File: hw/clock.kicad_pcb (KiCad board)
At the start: 2 copper layers, 1 part, among them U1 ATMEGA328PB-AU

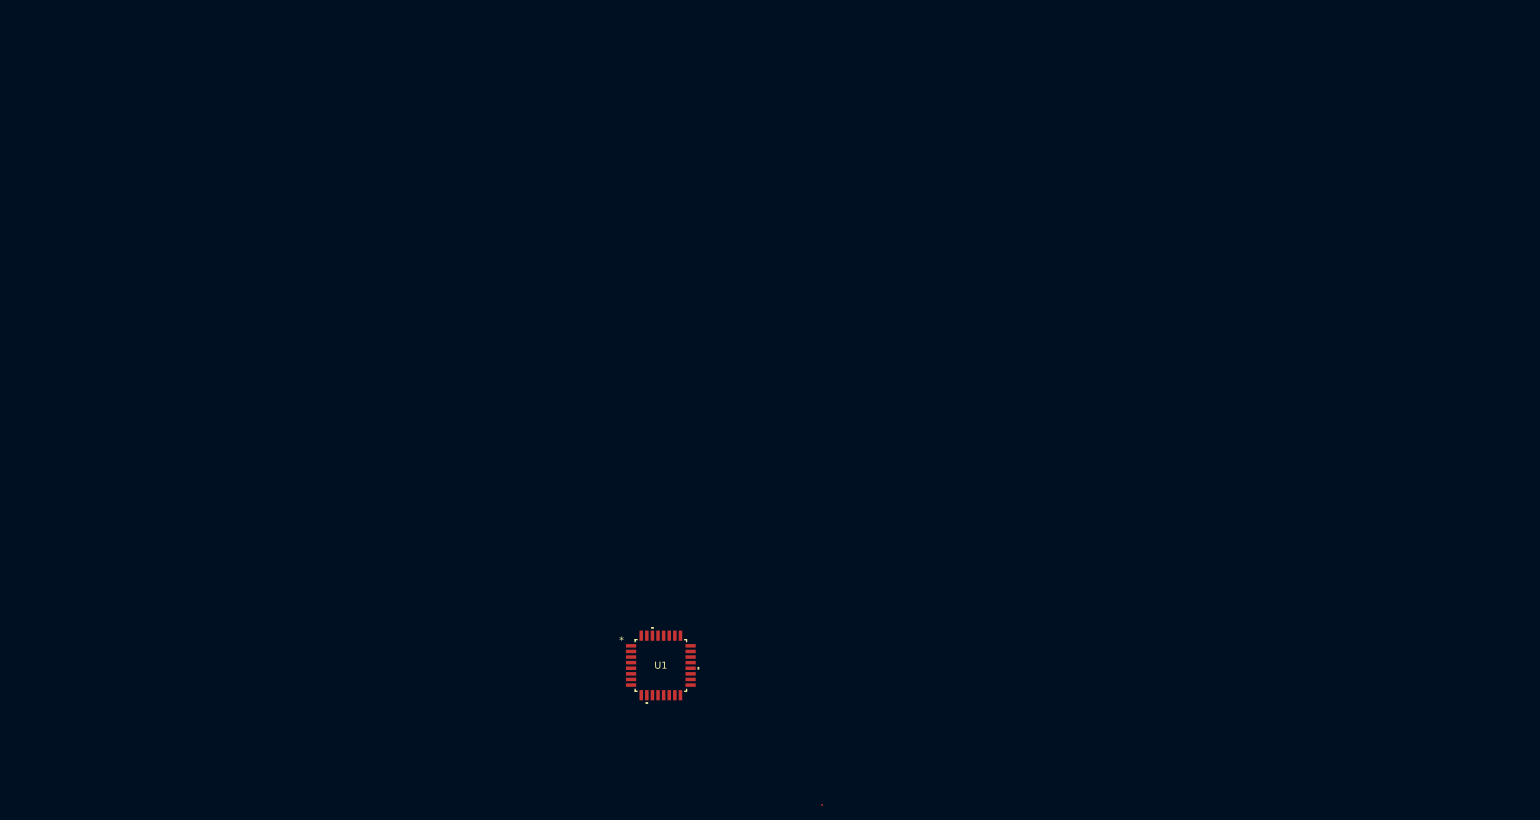
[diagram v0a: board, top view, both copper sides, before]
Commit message: Assign footprints
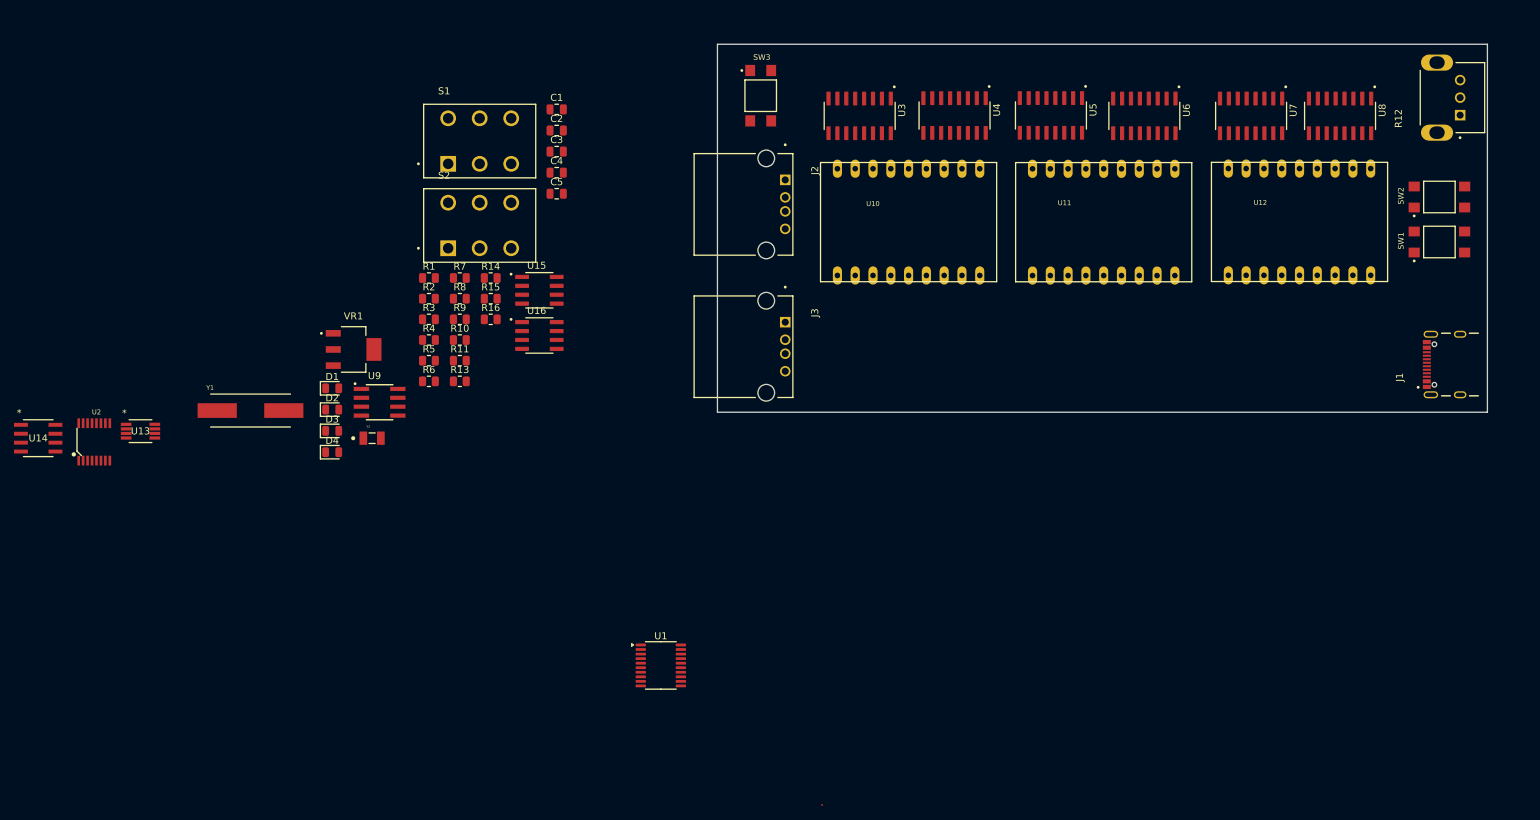
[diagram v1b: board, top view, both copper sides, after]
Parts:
- added C1: 18pf, Capacitor_SMD:C_0805_2012Metric, F.Cu at (117.4, 57.6)
- added C2: 18pf, Capacitor_SMD:C_0805_2012Metric, F.Cu at (117.4, 60.6)
- added C3: 12.5pf, Capacitor_SMD:C_0805_2012Metric, F.Cu at (117.4, 63.6)
- added C4: 12.5pf, Capacitor_SMD:C_0805_2012Metric, F.Cu at (117.4, 66.6)
- added C5: 33uf, Capacitor_SMD:C_0805_2012Metric, F.Cu at (117.4, 69.6)
- added D1: LED, LED_SMD:LED_0805_2012Metric, F.Cu at (85.4, 97.4)
- added D2: LED, LED_SMD:LED_0805_2012Metric, F.Cu at (85.4, 100.4)
- added D3: LED, LED_SMD:LED_0805_2012Metric, F.Cu at (85.4, 103.5)
- added D4: LED, LED_SMD:LED_0805_2012Metric, F.Cu at (85.4, 106.5)
- added J1: USB4105-GF-A, Clock:GCT_USB4105-GF-A, F.Cu at (246.4, 94.0)
- added J2: USB-A1HSW6, Clock:OST_USB-A1HSW6, F.Cu at (147.3, 71.1)
- added J3: USB-A1HSW6, Clock:OST_USB-A1HSW6, F.Cu at (147.3, 91.4)
- added R1: 10k, Resistor_SMD:R_0805_2012Metric, F.Cu at (99.2, 81.6)
- added R10: 10k, Resistor_SMD:R_0805_2012Metric, F.Cu at (103.6, 90.5)
- added R11: 10, Resistor_SMD:R_0805_2012Metric, F.Cu at (103.6, 93.4)
- added R12: PT01-B120D-B102, Clock:TRIM_PT01-B120D-B102, F.Cu at (243.1, 55.9)
- added R13: 10k, Resistor_SMD:R_0805_2012Metric, F.Cu at (103.6, 96.4)
- added R14: 10k, Resistor_SMD:R_0805_2012Metric, F.Cu at (108.0, 81.6)
- added R15: 2m, Resistor_SMD:R_0805_2012Metric, F.Cu at (108.0, 84.6)
- added R16: 2m, Resistor_SMD:R_0805_2012Metric, F.Cu at (108.0, 87.5)
- added R2: 5.1k, Resistor_SMD:R_0805_2012Metric, F.Cu at (99.2, 84.6)
- added R3: 5.1k, Resistor_SMD:R_0805_2012Metric, F.Cu at (99.2, 87.5)
- added R4: 10k, Resistor_SMD:R_0805_2012Metric, F.Cu at (99.2, 90.5)
- added R5: 10k, Resistor_SMD:R_0805_2012Metric, F.Cu at (99.2, 93.4)
- added R6: 10k, Resistor_SMD:R_0805_2012Metric, F.Cu at (99.2, 96.4)
- added R7: 10k, Resistor_SMD:R_0805_2012Metric, F.Cu at (103.6, 81.6)
- added R8: 10k, Resistor_SMD:R_0805_2012Metric, F.Cu at (103.6, 84.6)
- added R9: 10k, Resistor_SMD:R_0805_2012Metric, F.Cu at (103.6, 87.5)
- added S1: SLW-1678105-6A-N-D, Clock:SW_SLW-1678105-6A-N-D, F.Cu at (106.4, 62.1)
- added S2: SLW-1678105-6A-N-D, Clock:SW_SLW-1678105-6A-N-D, F.Cu at (106.4, 74.1)
- added SW1: TL3305AF260QG, Clock:SW_TL3305AF260QG, F.Cu at (243.4, 76.5)
- added SW2: TL3305AF260QG, Clock:SW_TL3305AF260QG, F.Cu at (243.4, 70.1)
- added SW3: TL3305AF260QG, Clock:SW_TL3305AF260QG, F.Cu at (146.5, 55.6)
- added U10: HDSP-5321 Common Anode, Clock:HDSP-R, F.Cu at (167.6, 73.6)
- added U11: HDSP-5321 Common Anode, Clock:HDSP-R, F.Cu at (195.5, 73.7)
- added U12: HDSP-5321 Common Anode, Clock:HDSP-R, F.Cu at (223.4, 73.6)
- added U13: MCP9808T-E/MS, Clock:MCP9808T, F.Cu at (58.0, 103.5)
- added U14: AP2192ASG-13, Clock:AP2192ASG_13, F.Cu at (43.4, 104.5)
- added U15: INA219AIDR, Clock:INA219AIDR, F.Cu at (114.9, 83.4)
- added U16: INA219AIDR, Clock:INA219AIDR, F.Cu at (114.9, 89.8)
- added U2: INTERFACE-FT230XS-R_SSOP16_, Clock:SSOP16-0.635-5X4MM, F.Cu at (51.4, 105.0)
- added U3: SN74HC595DR, Clock:SOIC127P600X175-16N, F.Cu at (160.7, 58.5)
- added U4: SN74HC595DR, Clock:SOIC127P600X175-16N, F.Cu at (174.2, 58.4)
- added U5: SN74HC595DR, Clock:SOIC127P600X175-16N, F.Cu at (188.0, 58.4)
- added U6: SN74HC595DR, Clock:SOIC127P600X175-16N, F.Cu at (201.3, 58.5)
- added U7: SN74HC595DR, Clock:SOIC127P600X175-16N, F.Cu at (216.5, 58.5)
- added U8: SN74HC595DR, Clock:SOIC127P600X175-16N, F.Cu at (229.2, 58.5)
- added U9: MCP7940MT-I_SN, Clock:SOIC127P600X175-8N, F.Cu at (92.1, 99.4)
- added VR1: LM3940IMP-3.3_NOPB, Clock:VREG_LM3940IMP-3.3_NOPB, F.Cu at (88.4, 91.8)
- added Y1: 30MHz, Clock:XTAL_ABLS2-30.000MHZ-D4YF-T, F.Cu at (73.7, 100.5)
- added Y2: 32.768KHz, Clock:XTAL_ECS-.327-12.5-34RR-TR, F.Cu at (91.1, 104.5)
- U1: value ATMEGA328PB-AU -> LPC812M101JDH20; footprint Clock:32A_MCH -> Package_SO:TSSOP-20_4.4x6.5mm_P0.65mm
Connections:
- U1 pad 1: unconnected-(U1-(OC2B/INT1/PTCXY)PD3-Pad1) -> SHIFT_SER_5
- U1 pad 10: unconnected-(U1-(OC0A/PTCXY/AIN0)PD6-Pad10) -> SHIFT_SER_4
- U1 pad 11: unconnected-(U1-(PTCXY/AIN1)PD7-Pad11) -> SHIFT_SER_3
- U1 pad 12: unconnected-(U1-(ICP1/CLKO/PTCXY)PB0-Pad12) -> MODE
- U1 pad 13: unconnected-(U1-(OC1A/PTCXY)PB1-Pad13) -> Net-(U1-PIO0_9)
- U1 pad 14: unconnected-(U1-(*SS0/OC1B/PTCXY)PB2-Pad14) -> Net-(U1-PIO0_8)
- U1 pad 15: unconnected-(U1-(MOSI0/TXD1/OC2A/PTCXY)PB3-Pad15) -> +3V3
- U1 pad 16: unconnected-(U1-(MISO0/RXD1/PTCXY)PB4-Pad16) -> +5V
- U1 pad 17: unconnected-(U1-(PTCXY/XCK1/SCK0)PB5-Pad17) -> SHIFT_SER_6
- U1 pad 18: unconnected-(U1-AVCC-Pad18) -> SHIFT_CLK
- U1 pad 19: unconnected-(U1-(ADC6/PTCY/ICP3/*SS1)PE2-Pad19) -> SERIAL1
- U1 pad 2: unconnected-(U1-(XCK0/T0/PTCXY)PD4-Pad2) -> SHIFT_SER_1
- U1 pad 20: unconnected-(U1-AREF-Pad20) -> SHIFT_SER_2
- U1 pad 3: unconnected-(U1-(SDA1/ICP4/ACO/PTCXY)PE0-Pad3) -> SHIFT_CLR
- U1 pad 4: unconnected-(U1-VCC-Pad4) -> RESET
- U1 pad 5: unconnected-(U1-GND-Pad5) -> SERIAL2
- U1 pad 6: unconnected-(U1-(SCL1/T4/PTCXY)PE1-Pad6) -> SHIFT_RCLK
- U1 pad 7: unconnected-(U1-(XTAL1/TOSC1)PB6-Pad7) -> RTC_PPS
- U1 pad 8: unconnected-(U1-(XTAL2/TOSC2)PB7-Pad8) -> SDA
- U1 pad 9: unconnected-(U1-(OC0B/T1/PTCXY)PD5-Pad9) -> SCL
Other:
- board outline added: 109.9 x 52.5 mm

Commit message: Minor schematic changes, routing
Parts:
- removed R2, R3: 5.1k, Resistor_SMD:R_0805_2012Metric
- added C10: 1uf, Capacitor_SMD:C_0805_2012Metric, F.Cu at (204.8, 132.1)
- added C6: 1uf, Capacitor_SMD:C_0805_2012Metric, F.Cu at (204.8, 120.0)
- added C7: 1uf, Capacitor_SMD:C_0805_2012Metric, F.Cu at (204.8, 123.0)
- added C8: 120uf, Capacitor_SMD:C_0805_2012Metric, F.Cu at (204.8, 126.1)
- added C9: 120uf, Capacitor_SMD:C_0805_2012Metric, F.Cu at (204.8, 129.1)
- C5: value 33uf -> 120uf
- J1: value USB4105-GF-A -> USB-A1HSW6; footprint Clock:GCT_USB4105-GF-A -> Clock:OST_USB-A1HSW6
- U14, U15, U16, U2, U9, Y2: moved to B.Cu
- moved U2 160.4 mm to (210.8, 87.8)
- moved Y1 127.9 mm to (201.3, 92.4), turned to -90 degrees
- moved U13 125.6 mm to (182.9, 90.0), turned to 90 degrees
- moved VR1 122.4 mm to (210.8, 90.0), turned to -90 degrees
- moved S2 121.4 mm to (226.6, 90.7)
- moved U14 114.0 mm to (154.9, 80.6), turned to 180 degrees
- moved Y2 109.1 mm to (199.4, 92.1), turned to -90 degrees
- moved U9 101.2 mm to (193.1, 92.1), turned to 180 degrees
- moved U1 77.5 mm to (194.0, 90.0)
- moved S1 68.1 mm to (168.2, 90.7)
- moved U16 44.2 mm to (154.9, 71.1)
- moved U15 40.9 mm to (155.0, 91.4)
- moved U5 16.6 mm to (189.0, 75.0)
- moved U6 16.6 mm to (202.3, 75.1)
- moved U3 16.6 mm to (161.3, 75.1)
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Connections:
- C1 pad 2: +5V -> GND
- C2 pad 1: +5V -> GND
- C3 pad 2: +5V -> GND
- C4 pad 1: +5V -> GND
- C5 pad 1: +5V -> GND
- D3 pad 1: +5V -> GND
- D4 pad 1: +5V -> GND
- J2 pad 4: +5V -> GND
- J3 pad 4: +5V -> GND
- R12 pad 3: +5V -> GND
- S1 pad 1: Net-(VR1-IN) -> unconnected-(S1-Pad1)
- S1 pad 3: unconnected-(S1-Pad3) -> Net-(VR1-IN)
- S1 pad 4: Net-(VR1-IN) -> unconnected-(S1-Pad4)
- S1 pad 6: unconnected-(S1-Pad6) -> Net-(VR1-IN)
- SW1 pad 1: +5V -> GND
- SW1 pad 2: +5V -> GND
- SW2 pad 1: +5V -> GND
- SW2 pad 2: +5V -> GND
- SW3 pad 1: +5V -> GND
- SW3 pad 2: +5V -> GND
- U1 pad 16: +5V -> GND
- U13 pad 4: +5V -> GND
- U13 pad 5: +5V -> GND
- U13 pad 6: +5V -> GND
- U13 pad 7: +5V -> GND
- U14 pad 1: +5V -> GND
- U15 pad 1: +5V -> +3V3
- U15 pad 2: +5V -> +3V3
- U15 pad 6: +5V -> GND
- U16 pad 1: +5V -> GND
- U16 pad 2: +5V -> GND
- U16 pad 6: +5V -> GND
- U2 pad 13: +5V -> GND
- U2 pad 5: +5V -> GND
- U2 pad 8: D+ -> Net-(J1-D+)
- U2 pad 9: D- -> Net-(J1-D-)
- U3 pad 13: +5V -> GND
- U3 pad 8: +5V -> GND
- U4 pad 13: +5V -> GND
- U4 pad 8: +5V -> GND
- U5 pad 13: +5V -> GND
- U5 pad 8: +5V -> GND
- U6 pad 13: +5V -> GND
- U6 pad 8: +5V -> GND
- U7 pad 13: +5V -> GND
- U7 pad 8: +5V -> GND
- U8 pad 13: +5V -> GND
- U8 pad 8: +5V -> GND
- U9 pad 4: +5V -> GND
- VR1 pad 2: +5V -> GND
- VR1 pad 4: +5V -> GND
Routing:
- net SHIFT_CLR: track 0.00 -> 98.5 mm
- net SHIFT_CLK: track 0.00 -> 93.5 mm, vias 0 -> 10
- net SHIFT_RCLK: track 0.00 -> 88.8 mm, vias 0 -> 10
- net SHIFT_SER_6: track 0.00 -> 41.6 mm
- net +3V3: track 0.00 -> 33.6 mm, vias 0 -> 6
- net SHIFT_SER_1: track 0.00 -> 32.7 mm, vias 0 -> 2
- net 5_A: track 0.00 -> 32.6 mm
- net 1_A: track 0.00 -> 32.6 mm
- net 3_A: track 0.00 -> 32.5 mm
- net 2_A: track 0.00 -> 32.4 mm
- net 6_A: track 0.00 -> 32.3 mm
- net 4_A: track 0.00 -> 32.2 mm
- net 1_G: track 0.00 -> 29.4 mm
- net 3_G: track 0.00 -> 28.6 mm
- net 5_G: track 0.00 -> 28.4 mm
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
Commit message: Place components
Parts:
- C3, C4, C6, C7, R13, R15, R16, R5: moved to B.Cu
- moved D2 168.8 mm to (253.1, 81.3)
- moved D1 156.8 mm to (241.3, 81.3), turned to -90 degrees
- moved R5 154.7 mm to (253.6, 84.8), turned to 180 degrees
- moved R4 146.2 mm to (245.1, 81.3), turned to 90 degrees
- moved R11 142.8 mm to (243.5, 65.0), turned to 180 degrees
- moved D3 141.4 mm to (226.6, 99.3)
- moved R1 137.8 mm to (237.0, 82.0), turned to 180 degrees
- moved R6 123.0 mm to (222.1, 99.1)
- moved C5 99.2 mm to (215.1, 87.0), turned to -90 degrees
- moved C2 93.4 mm to (205.0, 93.0), turned to -90 degrees
- moved C1 93.2 mm to (205.0, 89.4), turned to -90 degrees
- moved D4 88.6 mm to (173.6, 98.6)
- moved R10 85.4 mm to (188.7, 84.6), turned to 90 degrees
- moved R9 85.3 mm to (188.7, 93.2), turned to -90 degrees
- moved R7 83.9 mm to (186.7, 93.2), turned to -90 degrees
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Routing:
- net DISPLAY_PWR: track 0.00 -> 100.2 mm
- net SHIFT_CLR: track 98.5 -> 123.1 mm, vias 0 -> 2
- net +5V: track 0.00 -> 21.3 mm
- net GND: track 7.66 -> 27.1 mm
- net +3V3: track 33.6 -> 50.6 mm
- net Net-(U1-PIO0_9): track 0.00 -> 13.8 mm
- net Net-(U1-PIO0_8): track 0.00 -> 11.9 mm
- net Net-(R11-Pad1): track 0.00 -> 7.47 mm
- net RESET: track 0.00 -> 7.20 mm
- net SHIFT_SER_6: track 41.6 -> 42.6 mm

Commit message: Route top
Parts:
- C8, C9, R4: moved to B.Cu
- R13: moved to F.Cu
- moved R14 58.7 mm to (186.4, 94.5), turned to 180 degrees
- moved S1 58.4 mm to (226.6, 90.7)
- moved S2 58.4 mm to (168.2, 90.7)
- moved D4 23.8 mm to (156.0, 82.5), turned to -90 degrees
- moved D3 19.0 mm to (212.1, 87.1), turned to 90 degrees
- moved R5 18.6 mm to (235.2, 82.3), turned to 90 degrees
- moved D2 17.9 mm to (235.2, 82.2), turned to -90 degrees
- moved R6 14.2 mm to (214.4, 87.1), turned to 90 degrees
- moved C3 13.8 mm to (195.9, 98.3)
- moved R4 12.0 mm to (233.2, 82.3)
- moved C10 10.2 mm to (186.4, 96.5), turned to 180 degrees
- moved C9 9.91 mm to (183.6, 97.5)
- moved D1 8.18 mm to (233.2, 82.2)
- moved C4 8.18 mm to (190.5, 98.6)
- moved R9 5.34 mm to (186.4, 88.4), turned to 180 degrees
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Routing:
- net GND: track 27.1 -> 101.2 mm
- net +3V3: track 50.6 -> 88.0 mm
- net Net-(U14-EN1): track 0.00 -> 28.0 mm
- net Net-(VR1-IN): track 0.00 -> 26.4 mm
- net MODE: track 0.00 -> 25.5 mm, vias 0 -> 1
- net SDA: track 0.00 -> 14.2 mm, vias 0 -> 2
- net SCL: track 0.00 -> 12.7 mm, vias 0 -> 2
- net +5V: track 21.3 -> 27.8 mm
- net SHIFT_CLR: track 123.1 -> 128.1 mm
- net RTC_PPS: track 0.00 -> 4.85 mm
- net RESET: track 7.20 -> 11.6 mm
- net Net-(D3-A): track 0.00 -> 3.05 mm
- net Net-(D4-A): track 0.00 -> 2.28 mm
- net Net-(D2-K): track 0.00 -> 1.67 mm, vias 0 -> 1
- net Net-(D1-K): track 0.00 -> 1.67 mm, vias 0 -> 1

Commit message: Routed
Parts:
- moved C3 41.6 mm to (190.1, 57.1), turned to 0 degrees
- moved C4 38.9 mm to (190.0, 59.7)
- moved C8 36.8 mm to (159.6, 72.3)
- moved Y2 35.9 mm to (186.9, 58.4)
- moved U9 34.2 mm to (181.6, 59.7), turned to 180 degrees
- moved C9 25.5 mm to (159.6, 89.0), turned to -90 degrees
- moved C6 17.1 mm to (157.0, 72.3)
- moved C7 8.48 mm to (157.0, 89.0), turned to -90 degrees
- moved R15 7.49 mm to (154.5, 89.1), turned to 90 degrees
- moved R16 6.29 mm to (154.5, 72.3)
- moved U16 6.09 mm to (157.0, 76.8), turned to 180 degrees
- moved U2 4.09 mm to (212.6, 91.4)
- moved U14 3.64 mm to (157.0, 83.6)
- moved U15 2.96 mm to (157.0, 93.6), turned to 180 degrees
- turned R14 to 0 degrees
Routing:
- net +3V3: track 88.0 -> 342.6 mm, vias 6 -> 10
- net MODE: track 25.5 -> 113.0 mm, vias 1 -> 2
- net SCL: track 12.7 -> 99.0 mm, vias 2 -> 3
- net +5V: track 27.8 -> 101.0 mm, vias 0 -> 2
- net SDA: track 14.2 -> 83.6 mm
- net RESET: track 11.6 -> 77.9 mm, vias 0 -> 2
- net GND: track 101.2 -> 167.4 mm, vias 0 -> 13
- net Net-(U2-CBUS1): track 0.00 -> 41.4 mm, vias 0 -> 2
- net RTC_PPS: track 4.85 -> 41.8 mm, vias 0 -> 3
- net SHIFT_SER_5: track 0.00 -> 33.7 mm, vias 0 -> 2
- net Net-(J1-D+): track 0.00 -> 26.2 mm
- net Net-(J1-D-): track 0.00 -> 26.2 mm
- net Net-(U2-CBUS2): track 0.00 -> 23.9 mm
- net SERIAL2: track 0.00 -> 23.9 mm, vias 0 -> 1
- net USB_OUT2: track 0.00 -> 18.8 mm
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- added copper zone on B.Cu, net GND

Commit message: Routing and minor schematic changes
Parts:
- R13: value 10k -> 15k
- renumbered R12 to ADJ_BRIGHT, SW2 to BOOT, SW3 to MODE, D3 to ON, SW1 to RESET, D1 to RX, D2 to TX, D4 to USB_EN
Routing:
- net GND: track 167.4 -> 206.5 mm, vias 13 -> 15
- net +3V3: track 342.6 -> 350.9 mm
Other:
- board text added: "DSP1"
- board text added: "DSP2"
- board text added: "DSP3"
- board text added: "POWER"
- board text added: "USB"
- board text added: "USB_IN"
- board text added: "USB_OUT1"
- board text added: "USB_OUT2"

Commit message: Update hw
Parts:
- added C11: 47pf, Capacitor_SMD:C_0805_2012Metric, B.Cu at (239.2, 97.5)
- added C12: 47pf, Capacitor_SMD:C_0805_2012Metric, B.Cu at (239.2, 85.5)
- added C13: 10nf, Capacitor_SMD:C_0805_2012Metric, F.Cu at (217.0, 98.2)
- added R2: 27, Resistor_SMD:R_0805_2012Metric, B.Cu at (218.2, 90.5)
- added R3: 27, Resistor_SMD:R_0805_2012Metric, B.Cu at (218.2, 92.5)
- renumbered RX to D1, TX to D2, ON to D3, USB_EN to D4, ADJ_BRIGHT to R12, RESET to SW1, BOOT to SW2, MODE to SW3
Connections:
- U2 pad 8: Net-(J1-D+) -> Net-(U2-USBDP)
- U2 pad 9: Net-(J1-D-) -> Net-(U2-USBDM)
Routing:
- net GND: track 206.5 -> 186.9 mm
- net +5V: track 101.0 -> 106.8 mm
- net Net-(U2-USBDP): track 0.00 -> 3.23 mm
- net Net-(U2-USBDM): track 0.00 -> 3.18 mm
- net Net-(J1-D-): track 26.2 -> 27.0 mm
- net Net-(J1-D+): track 26.2 -> 27.0 mm
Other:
- board text added: "BOOT"
- board text added: "BRIGHT"
- board text added: "MODE"
- board text added: "PWR"
- board text added: "RESET"
- board text added: "RX"
- board text added: "TEMP"
- board text added: "TX"
- board text added: "USB_EN"

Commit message: Final touches
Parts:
- added ?: , , F.Cu at (242.0, 81.2)
- added ?: , , F.Cu at (238.2, 63.0)
- added ?: , , F.Cu at (179.0, 95.5)
- added G***: LOGO, LOGO, F.Cu at (157.0, 90.5)
- added R17: 0, Resistor_SMD:R_0805_2012Metric, F.Cu at (153.0, 71.2)
- added R18: 0, Resistor_SMD:R_0805_2012Metric, F.Cu at (153.0, 91.4)
- added REF**: MountingHole_2.2mm_M2_DIN965_Pad_TopOnly, MountingHole:MountingHole_2.2mm_M2_DIN965_Pad_TopOnly, F.Cu at (238.2, 63.0)
- added REF**: MountingHole_2.2mm_M2_DIN965_Pad_TopOnly, MountingHole:MountingHole_2.2mm_M2_DIN965_Pad_TopOnly, F.Cu at (242.0, 81.2)
- added REF**: MountingHole_2.2mm_M2_DIN965_Pad_TopOnly, MountingHole:MountingHole_2.2mm_M2_DIN965_Pad_TopOnly, F.Cu at (152.5, 56.0)
- added REF**: MountingHole_2.2mm_M2_DIN965_Pad_TopOnly, MountingHole:MountingHole_2.2mm_M2_DIN965_Pad_TopOnly, F.Cu at (179.0, 95.5)
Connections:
- J2 pad 2: unconnected-(J2-D--Pad2) -> Net-(J2-D-)
- J2 pad 3: unconnected-(J2-D+-Pad3) -> Net-(J2-D+)
- J3 pad 2: unconnected-(J3-D--Pad2) -> Net-(J3-D-)
- J3 pad 3: unconnected-(J3-D+-Pad3) -> Net-(J3-D+)
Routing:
- net Net-(J2-D-): track 0.00 -> 3.02 mm
- net Net-(J3-D+): track 0.00 -> 3.02 mm
- net Net-(J3-D-): track 0.00 -> 2.99 mm
- net Net-(J2-D+): track 0.00 -> 2.99 mm
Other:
- board text added: "5V OUT 1.5A MAX"
- board text added: "Y2"
